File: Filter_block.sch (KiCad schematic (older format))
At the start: 6 parts

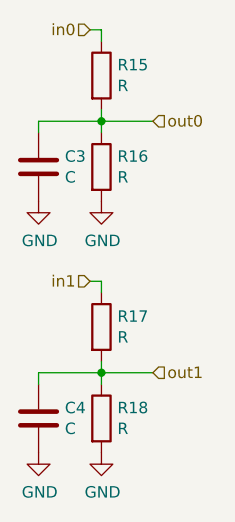
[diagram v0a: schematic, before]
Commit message: Motor Channel Cleanup
Removed some leftover labels in the motor channel after removal of the AND gate. Renumbering.
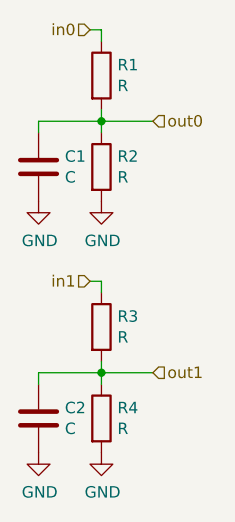
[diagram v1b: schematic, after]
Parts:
- renumbered C3 to C1, C4 to C2, R15 to R1, R16 to R2, R17 to R3, R18 to R4
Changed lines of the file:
@@
 AR Path="/596D7A67/5C1804A3/5C19820B/5BE230D0" Ref="R?"  Part="1"
 AR Path="/596D7A67/5C1804A3/5C1BC561/5BE230D0" Ref="R?"  Part="1"
-AR Path="/5E49E893/5E67E090/5BE230D0" Ref="R15"  Part="1"
-F 0 "R15" H 2920 1696 50  0000 L CNN
+AR Path="/5E49E893/5E67E090/5BE230D0" Ref="R1"  Part="1"
+F 0 "R1" H 2920 1696 50  0000 L CNN
 F 1 "R" H 2920 1605 50  0000 L CNN
 F 2 "Resistors_SMD:R_0603" V 2780 1650 50  0001 C CNN
@@
 AR Path="/596D7A67/5C1804A3/5C19820B/5BE23186" Ref="R?"  Part="1"
 AR Path="/596D7A67/5C1804A3/5C1BC561/5BE23186" Ref="R?"  Part="1"
-AR Path="/5E49E893/5E67E090/5BE23186" Ref="R16"  Part="1"
-F 0 "R16" H 2920 2096 50  0000 L CNN
+AR Path="/5E49E893/5E67E090/5BE23186" Ref="R2"  Part="1"
+F 0 "R2" H 2920 2096 50  0000 L CNN
 F 1 "R" H 2920 2005 50  0000 L CNN
 F 2 "Resistors_SMD:R_0603" V 2780 2050 50  0001 C CNN
@@
 AR Path="/596D7A67/5C1804A3/5C19820B/5BE231FF" Ref="C?"  Part="1"
 AR Path="/596D7A67/5C1804A3/5C1BC561/5BE231FF" Ref="C?"  Part="1"
-AR Path="/5E49E893/5E67E090/5BE231FF" Ref="C3"  Part="1"
-F 0 "C3" H 2690 2096 50  0000 L CNN
+AR Path="/5E49E893/5E67E090/5BE231FF" Ref="C1"  Part="1"
+F 0 "C1" H 2690 2096 50  0000 L CNN
 F 1 "C" H 2690 2005 50  0000 L CNN
 F 2 "Capacitors_SMD:C_0603" H 2613 1900 50  0001 C CNN
@@
 Data
 89 50 4E 47 0D 0A 1A 0A 00 00 00 0D 49 48 44 52 00 00 02 0B 00 00 00 94 08 03 00 00 00 2A 2E 9A
-43 00 00 00 03 73 42 49 54 08 08 08 DB E1 4F E0 00 00 00 30 50 4C 54 45 02 00 00 32 32 32 00 00
+43 00 00 00 03 73 42 49 54 08 08 08 DB E1 4F E0 00 00 00 30 50 4C 54 45 01 00 00 32 32 32 00 00
 00 10 10 10 76 76 76 CC CC CC AA AA AA 98 98 98 44 44 44 66 66 66 BA BA BA 22 22 22 DC DC DC 88
-88 88 54 54 54 EE EE EE 8F 1E 2E C9 00 00 00 01 74 52 4E 53 00 40 E6 D8 66 00 00 0B 6D 49 44 41
+88 88 54 54 54 EE EE EE C9 CC 1B AD 00 00 00 01 74 52 4E 53 00 40 E6 D8 66 00 00 0B 6D 49 44 41
 54 78 9C ED 9D E7 82 A3 20 10 80 03 08 36 CA FB BF ED 4A B2 2A D5 16 50 20 7C BF 2E 77 7B 59 07
 07 98 C6 F0 7A FD 38 00 AA 20 D0 E0 A7 9F 28 28 85 8B 17 16 4C DA 6E 1A A5 9E 0C C3 40 DA 66 1A
@@
 Data
 89 50 4E 47 0D 0A 1A 0A 00 00 00 0D 49 48 44 52 00 00 01 3B 00 00 00 92 08 03 00 00 00 0D 66 9D
-67 00 00 00 03 73 42 49 54 08 08 08 DB E1 4F E0 00 00 00 30 50 4C 54 45 02 00 00 DC DC DC BA BA
+67 00 00 00 03 73 42 49 54 08 08 08 DB E1 4F E0 00 00 00 30 50 4C 54 45 01 00 00 DC DC DC BA BA
 BA 10 10 10 44 44 44 88 88 88 00 00 00 CC CC CC 98 98 98 54 54 54 EE EE EE 32 32 32 AA AA AA 76
-76 76 66 66 66 22 22 22 CF 32 5B DC 00 00 00 01 74 52 4E 53 00 40 E6 D8 66 00 00 06 AF 49 44 41
+76 76 66 66 66 22 22 22 89 E0 6E B8 00 00 00 01 74 52 4E 53 00 40 E6 D8 66 00 00 06 AF 49 44 41
 54 78 9C ED 9D EB 9A A3 20 0C 86 8B 20 C8 49 EE FF 6E 57 9C 5A 05 83 16 56 A6 C5 C9 FB 63 9F 19
 DB 6D F5 9B 10 92 40 F4 F1 F8 93 90 EE D3 67 D0 2C 84 B2 4F 9F 42 AB F4 9C A3 76 F9 10 31 48 CA
@@
 AR Path="/596D7A67/5C1804A3/5C19820B/5BE232A5" Ref="#PWR?"  Part="1"
 AR Path="/596D7A67/5C1804A3/5C1BC561/5BE232A5" Ref="#PWR?"  Part="1"
-AR Path="/5E49E893/5E67E090/5BE232A5" Ref="#PWR032"  Part="1"
-F 0 "#PWR032" H 2850 1950 50  0001 C CNN
+AR Path="/5E49E893/5E67E090/5BE232A5" Ref="#PWR06"  Part="1"
+F 0 "#PWR06" H 2850 1950 50  0001 C CNN
 F 1 "GND" H 2855 2027 50  0000 C CNN
 F 2 "" H 2850 2200 50  0001 C CNN
@@
 AR Path="/596D7A67/5C1804A3/5C19820B/5BE2328D" Ref="#PWR?"  Part="1"
 AR Path="/596D7A67/5C1804A3/5C1BC561/5BE2328D" Ref="#PWR?"  Part="1"
-AR Path="/5E49E893/5E67E090/5BE2328D" Ref="#PWR030"  Part="1"
-F 0 "#PWR030" H 2575 1950 50  0001 C CNN
+AR Path="/5E49E893/5E67E090/5BE2328D" Ref="#PWR04"  Part="1"
+F 0 "#PWR04" H 2575 1950 50  0001 C CNN
 F 1 "GND" H 2580 2027 50  0000 C CNN
 F 2 "" H 2575 2200 50  0001 C CNN
@@
 AR Path="/596D7A67/5C1804A3/5C19820B/5BE25BE7" Ref="R?"  Part="1"
 AR Path="/596D7A67/5C1804A3/5C1BC561/5BE25BE7" Ref="R?"  Part="1"
-AR Path="/5E49E893/5E67E090/5BE25BE7" Ref="R17"  Part="1"
-F 0 "R17" H 2920 2796 50  0000 L CNN
+AR Path="/5E49E893/5E67E090/5BE25BE7" Ref="R3"  Part="1"
+F 0 "R3" H 2920 2796 50  0000 L CNN
 F 1 "R" H 2920 2705 50  0000 L CNN
 F 2 "Resistors_SMD:R_0603" V 2780 2750 50  0001 C CNN
@@
 AR Path="/596D7A67/5C1804A3/5C19820B/5BE25BEE" Ref="R?"  Part="1"
 AR Path="/596D7A67/5C1804A3/5C1BC561/5BE25BEE" Ref="R?"  Part="1"
-AR Path="/5E49E893/5E67E090/5BE25BEE" Ref="R18"  Part="1"
-F 0 "R18" H 2920 3196 50  0000 L CNN
+AR Path="/5E49E893/5E67E090/5BE25BEE" Ref="R4"  Part="1"
+F 0 "R4" H 2920 3196 50  0000 L CNN
 F 1 "R" H 2920 3105 50  0000 L CNN
 F 2 "Resistors_SMD:R_0603" V 2780 3150 50  0001 C CNN
@@
 AR Path="/596D7A67/5C1804A3/5C19820B/5BE25BF5" Ref="C?"  Part="1"
 AR Path="/596D7A67/5C1804A3/5C1BC561/5BE25BF5" Ref="C?"  Part="1"
-AR Path="/5E49E893/5E67E090/5BE25BF5" Ref="C4"  Part="1"
-F 0 "C4" H 2690 3196 50  0000 L CNN
+AR Path="/5E49E893/5E67E090/5BE25BF5" Ref="C2"  Part="1"
+F 0 "C2" H 2690 3196 50  0000 L CNN
 F 1 "C" H 2690 3105 50  0000 L CNN
 F 2 "Capacitors_SMD:C_0603" H 2613 3000 50  0001 C CNN
@@
 AR Path="/596D7A67/5C1804A3/5C19820B/5BE25C06" Ref="#PWR?"  Part="1"
 AR Path="/596D7A67/5C1804A3/5C1BC561/5BE25C06" Ref="#PWR?"  Part="1"
-AR Path="/5E49E893/5E67E090/5BE25C06" Ref="#PWR033"  Part="1"
-F 0 "#PWR033" H 2850 3050 50  0001 C CNN
+AR Path="/5E49E893/5E67E090/5BE25C06" Ref="#PWR07"  Part="1"
+F 0 "#PWR07" H 2850 3050 50  0001 C CNN
 F 1 "GND" H 2855 3127 50  0000 C CNN
 F 2 "" H 2850 3300 50  0001 C CNN
@@
 AR Path="/596D7A67/5C1804A3/5C19820B/5BE25C0C" Ref="#PWR?"  Part="1"
 AR Path="/596D7A67/5C1804A3/5C1BC561/5BE25C0C" Ref="#PWR?"  Part="1"
-AR Path="/5E49E893/5E67E090/5BE25C0C" Ref="#PWR031"  Part="1"
-F 0 "#PWR031" H 2575 3050 50  0001 C CNN
+AR Path="/5E49E893/5E67E090/5BE25C0C" Ref="#PWR05"  Part="1"
+F 0 "#PWR05" H 2575 3050 50  0001 C CNN
 F 1 "GND" H 2580 3127 50  0000 C CNN
 F 2 "" H 2575 3300 50  0001 C CNN
